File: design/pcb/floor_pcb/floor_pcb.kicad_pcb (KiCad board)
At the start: 2 copper layers, 75 x 210 mm, 11 parts, among them J1 Conn_01x10_Male, J10 shock_grid, J11 shock_grid, J2 Conn_01x10_Male, J3 Conn_02x10_Top_Bottom, J4 shock_grid, J5 shock_grid, J6 shock_grid, J7 shock_grid, J8 shock_grid, J9 shock_grid

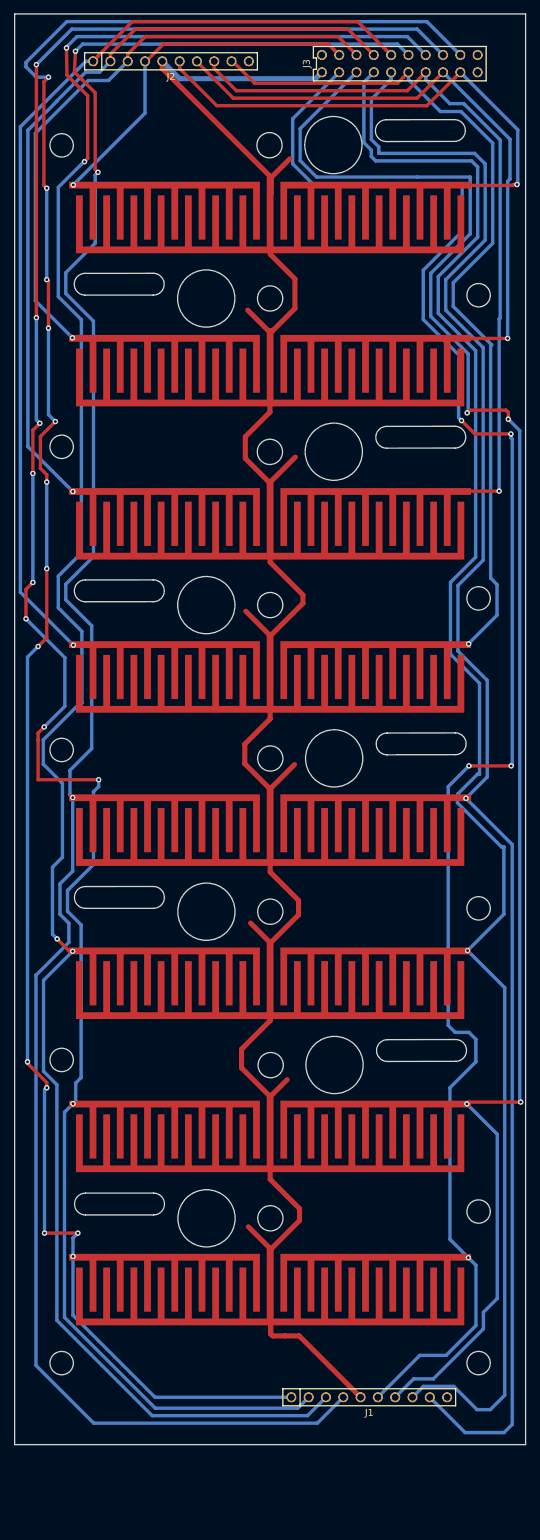
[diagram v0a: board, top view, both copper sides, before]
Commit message: Redid some of floor PCB. Added 25pin DSub connector. Deleted old design files with one layer per file. Moved slider compressors (rails) to main file as blocks in their own layer. Added initial README explaining different lasercut design files.
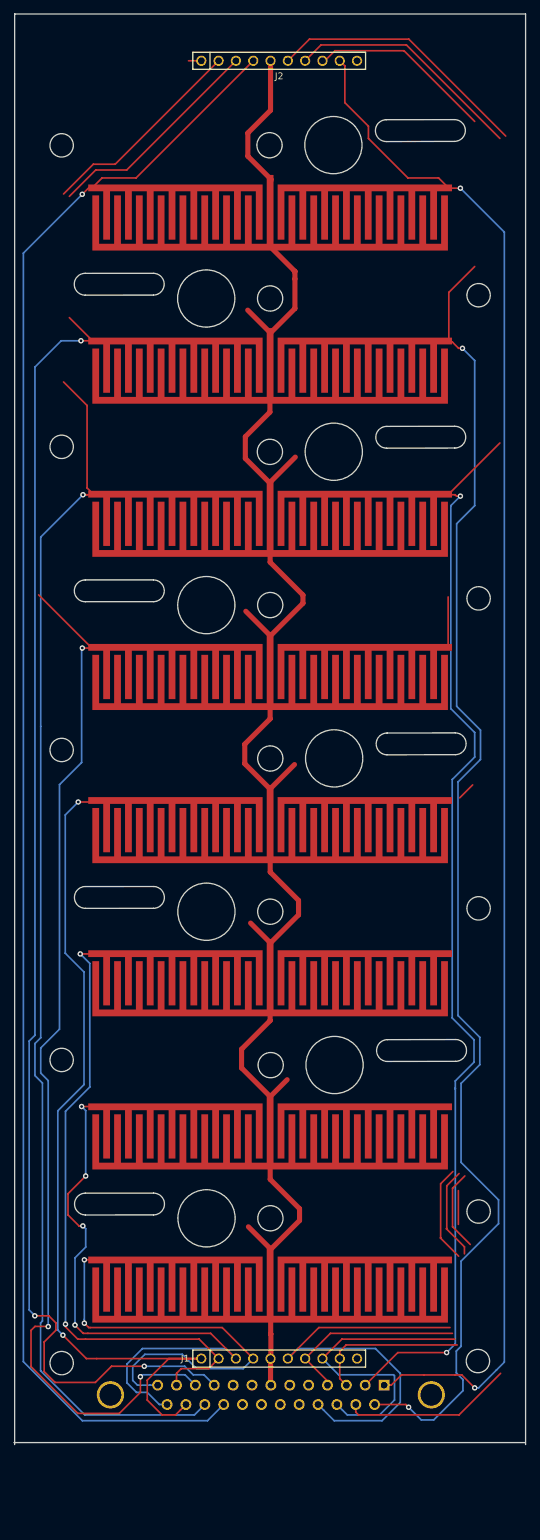
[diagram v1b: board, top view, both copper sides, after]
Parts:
- J10, J11, J4, J5, J6, J7, J8, J9: footprint footprints:electrode -> footprints:electrodes_clearance0.6mm
- J3: value Conn_02x10_Top_Bottom -> DB25_Male; footprint footprints:DIP-2x10_2.54mm_1mm_clearance -> Connectors_DSub:DSUB-25_Male_Horizontal_Pitch2.77x2.84mm_EdgePinOffset7.70mm_Housed_MountingHolesOffset9.12mm; moved to B.Cu
- moved J3 194.0 mm to (141.7, 207.8), turned to 180 degrees
- moved J2 15.9 mm to (126.3, 13.4)
- moved J1 14.4 mm to (126.3, 203.9)
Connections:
- J1 pad 1: Net-(J1-Pad1) -> /F7
- J1 pad 2: Net-(J1-Pad2) -> /F5
- J1 pad 3: Net-(J1-Pad3) -> /F3
- J1 pad 4: Net-(J1-Pad4) -> /F1
- J1 pad 5: Net-(J1-Pad5) -> /HV
- J1 pad 6: Net-(J1-Pad6) -> /F2
- J1 pad 7: Net-(J1-Pad7) -> /F4
- J1 pad 8: Net-(J1-Pad8) -> /F6
- J1 pad 9: Net-(J1-Pad9) -> /F8
- J10 pad 0: Net-(J1-Pad5) -> /HV
- J10 pad 1: Net-(J10-Pad1) -> /F14
- J10 pad 2: Net-(J10-Pad2) -> /F13
- J11 pad 0: Net-(J1-Pad5) -> /HV
- J11 pad 1: Net-(J11-Pad1) -> /F16
- J11 pad 2: Net-(J11-Pad2) -> /F15
- J2 pad 1: Net-(J2-Pad1) -> /F9
- J2 pad 2: Net-(J2-Pad2) -> /F11
- J2 pad 3: Net-(J10-Pad2) -> /F13
- J2 pad 4: Net-(J11-Pad2) -> /F15
- J2 pad 5: Net-(J1-Pad5) -> /HV
- J2 pad 6: Net-(J11-Pad1) -> /F10
- J2 pad 7: Net-(J10-Pad1) -> /F12
- J2 pad 8: Net-(J2-Pad8) -> /F14
- J2 pad 9: Net-(J2-Pad9) -> /F16
- J3 pad 1: Net-(J1-Pad5) -> /F16
- J3 pad 10: Net-(J3-Pad10) -> /F13
- J3 pad 11: Net-(J3-Pad11) -> /F9
- J3 pad 12: Net-(J1-Pad1) -> /F5
- J3 pad 13: Net-(J1-Pad2) -> /F1
- J3 pad 14: Net-(J1-Pad3) -> /F14
- J3 pad 15: Net-(J1-Pad4) -> /F10
- J3 pad 16: Net-(J2-Pad1) -> /F6
- J3 pad 17: Net-(J2-Pad2) -> /F2
- J3 pad 18: Net-(J10-Pad2) -> Net-(J3-Pad18)
- J3 pad 19: Net-(J11-Pad2) -> Net-(J3-Pad19)
- J3 pad 2: Net-(J1-Pad6) -> /F12
- J3 pad 3: Net-(J1-Pad7) -> /F8
- J3 pad 4: Net-(J1-Pad8) -> /F4
- J3 pad 5: Net-(J1-Pad9) -> Net-(J3-Pad5)
- J3 pad 6: Net-(J2-Pad9) -> Net-(J3-Pad6)
- J3 pad 7: Net-(J2-Pad8) -> /HV
- J3 pad 8: Net-(J10-Pad1) -> Net-(J3-Pad8)
- J3 pad 9: Net-(J11-Pad1) -> Net-(J3-Pad9)
- J4 pad 0: Net-(J1-Pad5) -> /HV
- J4 pad 1: Net-(J1-Pad6) -> /F2
- J4 pad 2: Net-(J1-Pad1) -> /F1
- J5 pad 0: Net-(J1-Pad5) -> /HV
- J5 pad 1: Net-(J1-Pad7) -> /F4
- J5 pad 2: Net-(J1-Pad2) -> /F3
- J6 pad 0: Net-(J1-Pad5) -> /HV
- J6 pad 1: Net-(J1-Pad8) -> /F6
- J6 pad 2: Net-(J1-Pad3) -> /F5
- J7 pad 0: Net-(J1-Pad5) -> /HV
- J7 pad 1: Net-(J1-Pad9) -> /F8
- J7 pad 2: Net-(J1-Pad4) -> /F7
- J8 pad 0: Net-(J1-Pad5) -> /HV
- J8 pad 1: Net-(J2-Pad9) -> /F10
- J8 pad 2: Net-(J2-Pad1) -> /F9
- J9 pad 0: Net-(J1-Pad5) -> /HV
- J9 pad 1: Net-(J2-Pad8) -> /F12
- J9 pad 2: Net-(J2-Pad2) -> /F11
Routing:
- net Net-(J1-Pad2): track 307.0 -> 0.00 mm, vias 9 -> 0
- net Net-(J1-Pad4): track 306.3 -> 0.00 mm, vias 3 -> 0
- net Net-(J1-Pad3): track 303.6 -> 0.00 mm, vias 4 -> 0
- net Net-(J1-Pad1): track 301.6 -> 0.00 mm, vias 13 -> 0
- net Net-(J1-Pad5): track 297.5 -> 0.00 mm
- net Net-(J1-Pad6): track 253.3 -> 0.00 mm, vias 5 -> 0
- net Net-(J1-Pad7): track 250.9 -> 0.00 mm, vias 4 -> 0
- net Net-(J1-Pad8): track 243.5 -> 0.00 mm, vias 1 -> 0
- net /F15: track 0.00 -> 242.1 mm, vias 0 -> 1
- net Net-(J1-Pad9): track 241.7 -> 0.00 mm, vias 1 -> 0
- net /F13: track 0.00 -> 226.7 mm, vias 0 -> 3
- net /F16: track 0.00 -> 225.3 mm, vias 0 -> 2
- net /F14: track 0.00 -> 223.4 mm, vias 0 -> 2
- net /F11: track 0.00 -> 209.8 mm, vias 0 -> 1
- net /F12: track 0.00 -> 194.1 mm, vias 0 -> 2
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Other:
- board size 75 x 210 mm -> 75.1 x 210 mm

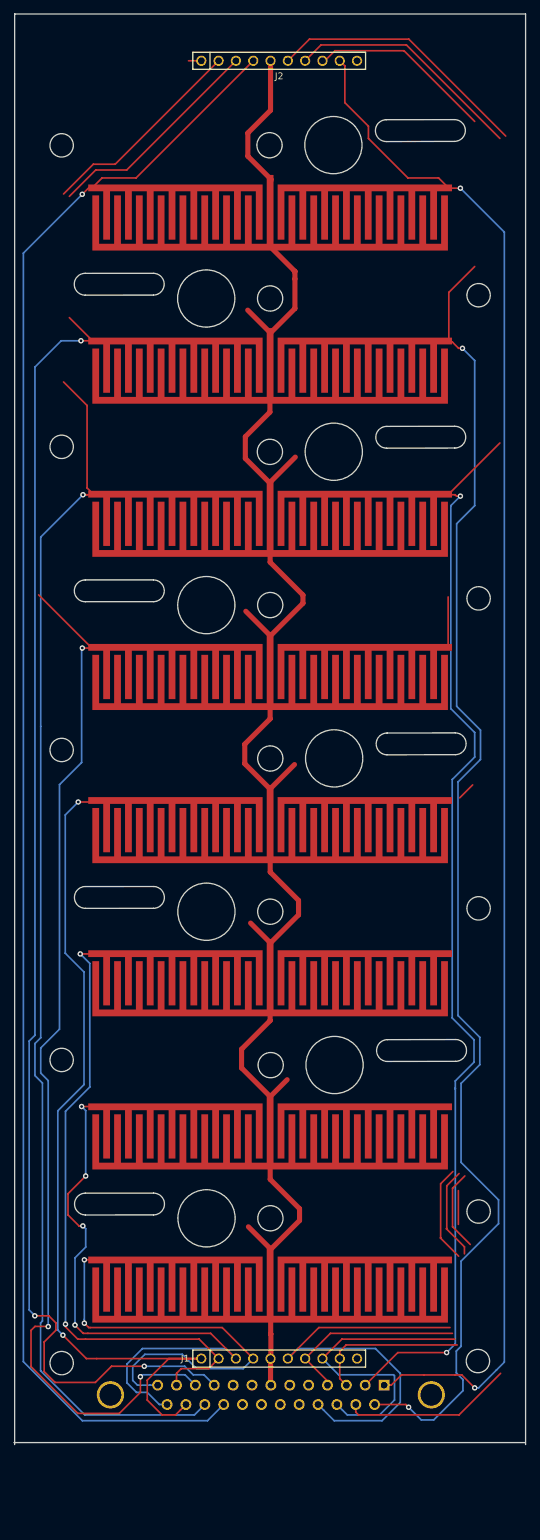
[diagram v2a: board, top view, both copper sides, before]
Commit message: Seem to have make_board working to align top and bottom connectors, and J3 on the bottom, but I need to pick different offsets from nearest grid for top and bottom. May need to make ceiling board a little longer on the top. ADD EXTRA MOUNTING HOLES IN BOTTOM.
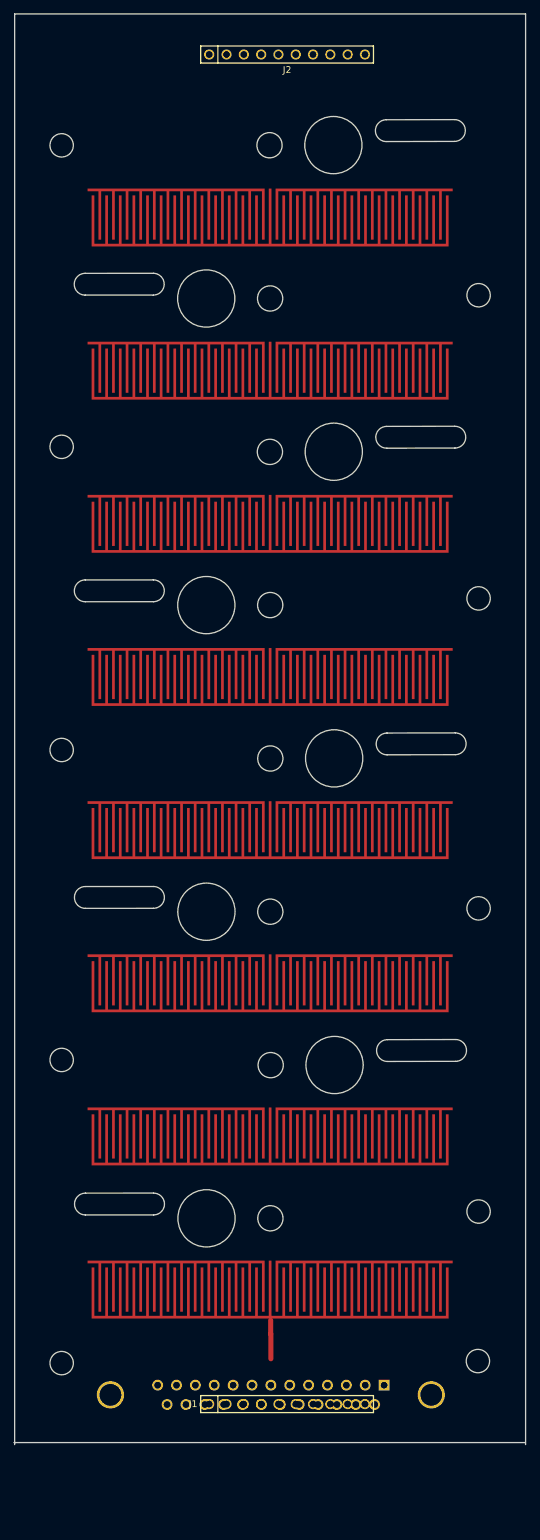
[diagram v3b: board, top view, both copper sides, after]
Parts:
- J10, J11, J4, J5, J6, J7, J8, J9: footprint footprints:electrodes_clearance0.6mm -> footprints:electrodes_clearance0.6mm_W0.4mm_centerflush
- moved J1 6.78 mm to (127.5, 210.6)
- moved J2 1.48 mm to (127.5, 12.5)
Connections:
- J1 pad 1: /F7 -> /F9
- J1 pad 2: /F5 -> /F11
- J1 pad 3: /F3 -> /F13
- J1 pad 4: /F1 -> /F15
- J1 pad 6: /F2 -> /F16
- J1 pad 7: /F4 -> /F14
- J1 pad 8: /F6 -> /F12
- J1 pad 9: /F8 -> /F10
- J10 pad 1: /F14 -> /F4
- J10 pad 2: /F13 -> /F3
- J11 pad 1: /F16 -> /F2
- J11 pad 2: /F15 -> /F1
- J2 pad 1: /F9 -> /F7
- J2 pad 2: /F11 -> /F5
- J2 pad 3: /F13 -> /F3
- J2 pad 4: /F15 -> /F1
- J2 pad 6: /F10 -> /F2
- J2 pad 7: /F12 -> /F4
- J2 pad 8: /F14 -> /F6
- J2 pad 9: /F16 -> /F8
- J4 pad 1: /F2 -> /F16
- J4 pad 2: /F1 -> /F15
- J5 pad 1: /F4 -> /F14
- J5 pad 2: /F3 -> /F13
- J6 pad 1: /F6 -> /F12
- J6 pad 2: /F5 -> /F11
- J7 pad 1: /F8 -> /F10
- J7 pad 2: /F7 -> /F9
- J8 pad 1: /F10 -> /F8
- J8 pad 2: /F9 -> /F7
- J9 pad 1: /F12 -> /F6
- J9 pad 2: /F11 -> /F5
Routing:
- net /F15: track 242.1 -> 0.00 mm, vias 1 -> 0
- net /F13: track 226.7 -> 0.00 mm, vias 3 -> 0
- net /F16: track 225.3 -> 0.00 mm, vias 2 -> 0
- net /F14: track 223.4 -> 0.00 mm, vias 2 -> 0
- net /F11: track 209.8 -> 0.00 mm, vias 1 -> 0
- net /F12: track 194.1 -> 0.00 mm, vias 2 -> 0
- net /HV: track 172.0 -> 5.62 mm
- net /F9: track 156.3 -> 0.00 mm, vias 3 -> 0
- net /F7: track 125.1 -> 0.00 mm, vias 2 -> 0
- net /F5: track 91.7 -> 0.00 mm, vias 2 -> 0
- net /F3: track 90.3 -> 0.00 mm, vias 4 -> 0
- net /F10: track 79.4 -> 0.00 mm
- net /F1: track 63.2 -> 0.00 mm, vias 2 -> 0
- net /F2: track 62.7 -> 0.00 mm
- net /F6: track 59.4 -> 0.00 mm
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
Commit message: v0.1 boards done. Decided not to add LEDs to shield board for now.
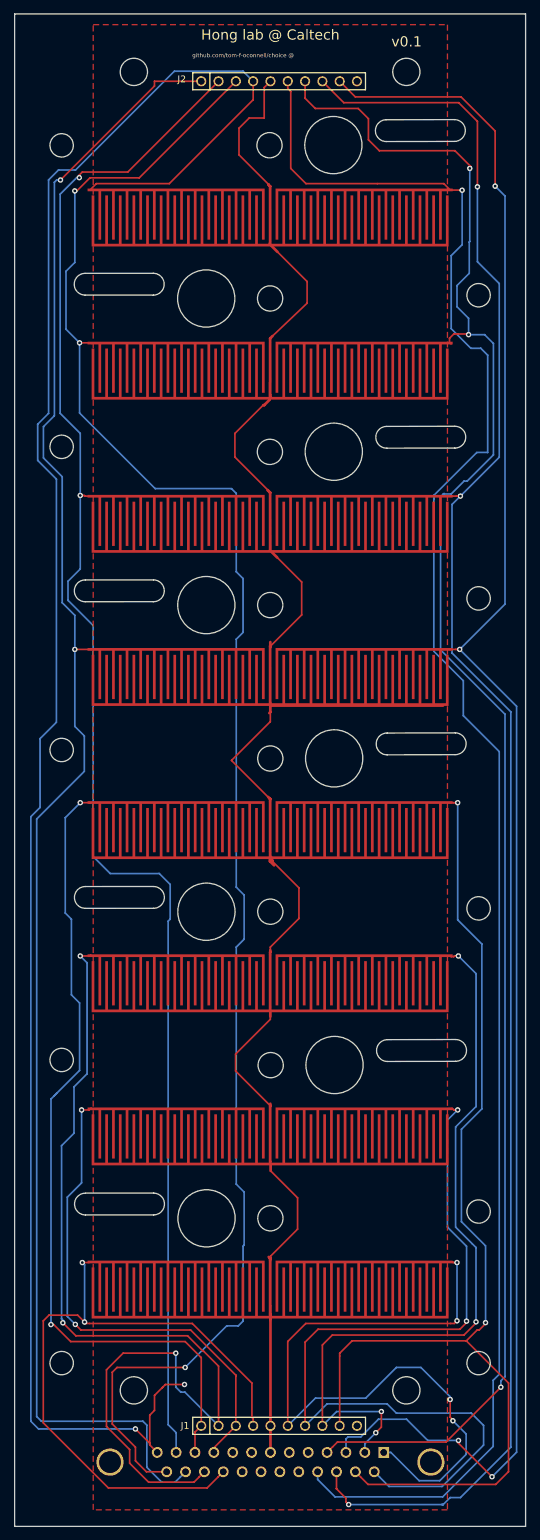
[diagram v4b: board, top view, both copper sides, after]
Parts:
- moved J3 9.87 mm to (141.7, 217.7)
- moved J2 4.10 mm to (126.3, 16.4)
- moved J1 3.40 mm to (126.3, 213.8)
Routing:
- net /F1: track 0.00 -> 288.3 mm, vias 0 -> 2
- net /HV: track 5.62 -> 282.3 mm
- net /F2: track 0.00 -> 267.3 mm, vias 0 -> 1
- net /F6: track 0.00 -> 262.2 mm, vias 0 -> 3
- net /F8: track 0.00 -> 261.9 mm, vias 0 -> 4
- net /F3: track 0.00 -> 259.8 mm, vias 0 -> 3
- net /F4: track 0.00 -> 258.3 mm, vias 0 -> 3
- net /F7: track 0.00 -> 248.2 mm, vias 0 -> 2
- net /F5: track 0.00 -> 229.5 mm, vias 0 -> 2
- net /F10: track 0.00 -> 161.6 mm, vias 0 -> 2
- net /F11: track 0.00 -> 144.6 mm, vias 0 -> 3
- net /F14: track 0.00 -> 122.7 mm, vias 0 -> 2
- net /F9: track 0.00 -> 120.4 mm, vias 0 -> 2
- net /F12: track 0.00 -> 111.0 mm, vias 0 -> 4
- net /F16: track 0.00 -> 102.2 mm, vias 0 -> 4
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- added copper zone on F.Cu, net /HV
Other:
- board size 75.1 x 210 mm -> 75 x 222 mm
- board text added: "Be cautious with heat in particularly the back copper traces, in cases where the heat from a shorted chamber might affect the behavior of a fly in another chamber. Maybe fix if redesigning, though might need to make wider."
- board text added: "Hong lab @ Caltech"
- board text added: "Though the FR4 substrate for the current bottom acts as a diffuser for the IR backlights, substrates that transmit more IR are probably desirable. We should have been using 850nm backlights."
- board text added: "github.com/tom-f-oconnell/choice @"
- board text added: "v0.1"

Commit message: Generated initial gerbers. Going to test against Advanced Circuits system.
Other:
- board text added: "Board should be 1/16" thick (1.5875 mm)"
- board text added: "github.com/tom-f-oconnell/choice @ d141ec9f"
- board text removed: "github.com/tom-f-oconnell/choice @"
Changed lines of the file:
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@@
   (general
     (thickness 1.6)
-    (drawings 71)
+    (drawings 72)
     (tracks 582)
     (zones 0)
@@
     (title "8 chamber shock conditioning floor grid")
     (date 06-12-2017)
+    (rev 0.1)
     (company "Hong Lab @ Caltech")
   )
@@
     (visible_elements FFFFFF7F)
     (pcbplotparams
-      (layerselection 0x00030_ffffffff)
+      (layerselection 0x01030_ffffffff)
       (usegerberextensions false)
       (usegerberattributes true)
@@
       (psa4output false)
       (plotreference true)
-      (plotvalue true)
+      (plotvalue false)
       (plotinvisibletext false)
       (padsonsilk false)
@@
       (drillshape 0)
       (scaleselection 1)
-      (outputdirectory ""))
+      (outputdirectory ../gerber/floor_pcb/))
   )
   (net 0 "")
@@
       ))
   )
-  (gr_text "github.com/tom-f-oconnell/choice @ " (at 121.03 12.58) (layer F.SilkS)
+  (gr_text "Board should be 1/16\" thick (1.5875 mm)" (at 49.53 97.08) (layer Cmts.User)
+    (effects (font (size 1.5 1.5) (thickness 0.3)))
+  )
+  (gr_text "github.com/tom-f-oconnell/choice @ d141ec9f" (at 125.03 12.58) (layer F.SilkS)
     (effects (font (size 0.6 0.6) (thickness 0.1)))
   )
@@
     (effects (font (size 1.5 1.5) (thickness 0.3)))
   )
-  (gr_text "Though the FR4 substrate for the current bottom\nacts as a diffuser for the IR backlights, substrates\nthat transmit more IR are probably desirable.\n\nWe should have been using 850nm backlights." (at 49.03 215.08) (layer B.Fab)
+  (gr_text "Though the FR4 substrate for the current bottom\nacts as a diffuser for the IR backlights, substrates\nthat transmit more IR are probably desirable.\n\nWe should have been using 850nm backlights." (at 48.53 121.08) (layer B.Fab)
     (effects (font (size 1.5 1.5) (thickness 0.3)))
   )
